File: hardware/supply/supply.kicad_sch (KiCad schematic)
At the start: 33 parts, among them J1 Conn_01x01, J2 Screw, J3 Conn_01x01, J5 Conn_01x01, J6 Screw, J7 Conn_01x01, Q3 IRF4905PBF, Q4 BC857C, Q5 IRF4905PBF, Q6 IRF4905PBF, T1 TST160 19V-19V - 727 (4.21A)

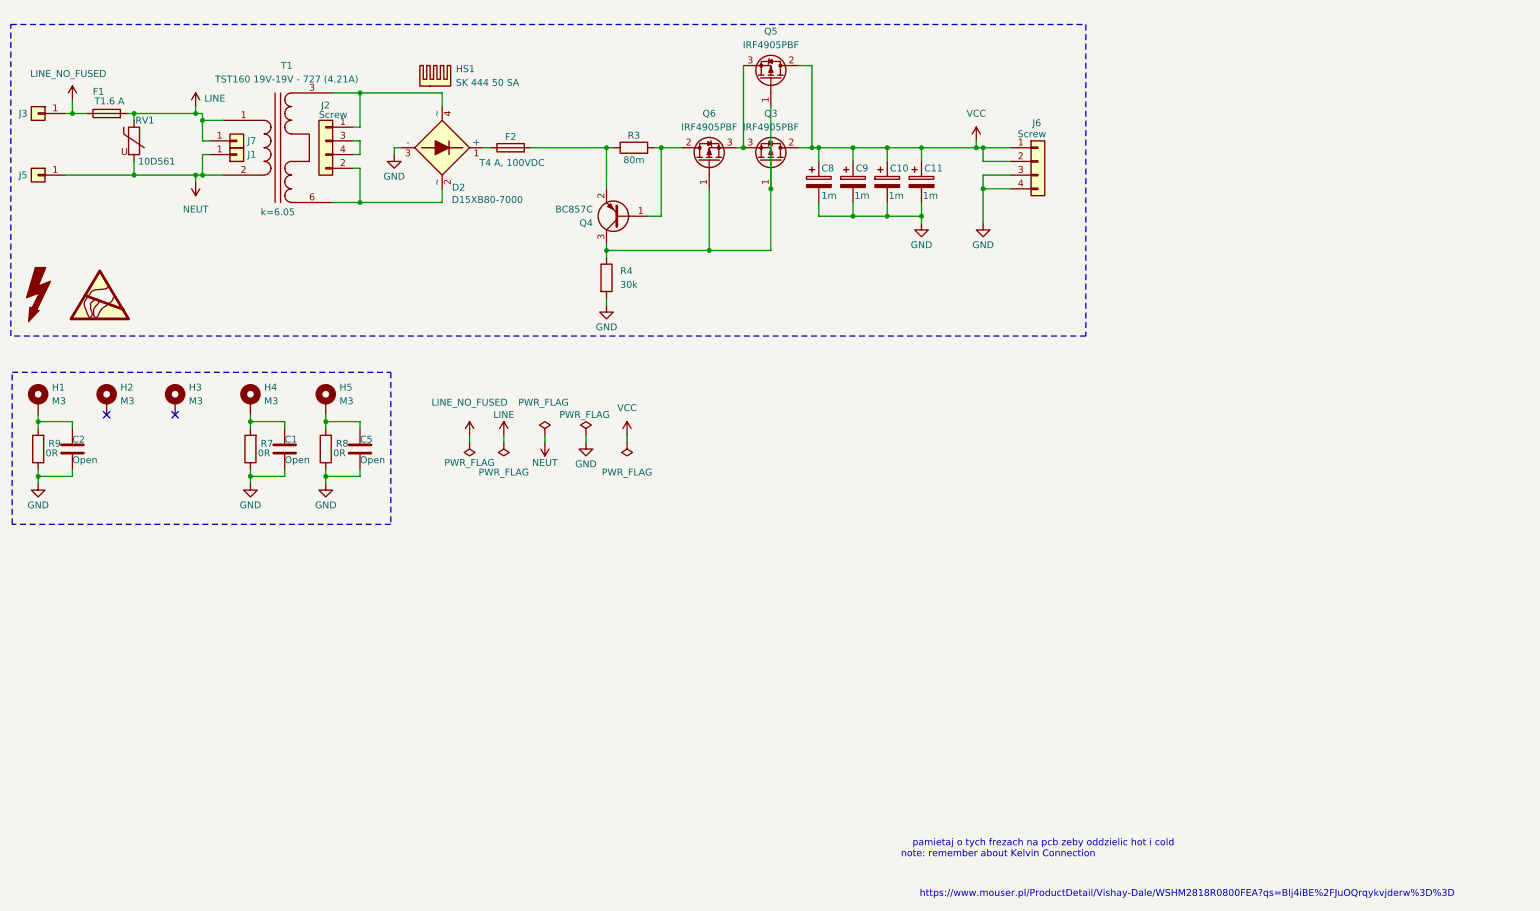
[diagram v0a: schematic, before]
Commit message: replace mosfets with bjts in inrush current limiter
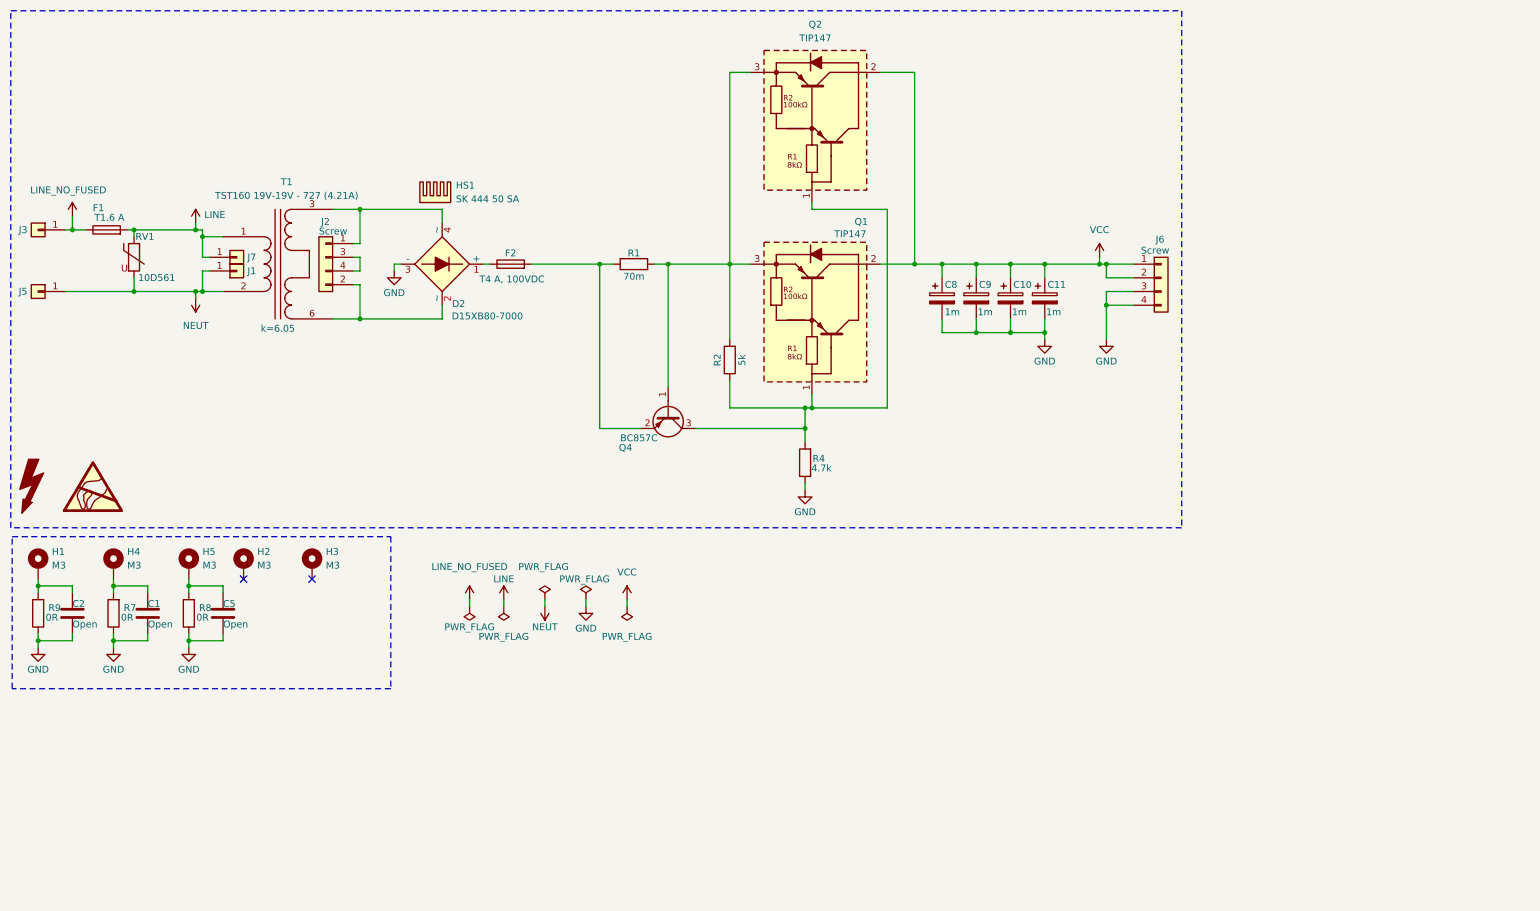
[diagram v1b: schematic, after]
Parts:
- removed Q3, Q5, Q6: IRF4905PBF, Package_TO_SOT_THT:TO-220-3_Vertical, symbol Transistor_FET:IRF4905
- removed R3: 80m, supply:WSHM28181L000FEA, symbol Device:R
- added Q1, Q2: TIP147, supply:TO545P515X1560X2445-3P, symbol supply:TIP147
- added R1: 70m, symbol Device:R
- added R2: 5k, Resistor_SMD:R_0805_2012Metric, symbol Device:R
- R4: value 30k -> 4.7k; footprint Resistor_SMD:R_1206_3216Metric -> Resistor_SMD:R_0805_2012Metric
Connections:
- net GND: now also R4.1; no longer R4.2
- net VCC: now also Q1.2 (C), Q2.2 (C)
- net at Q4.3 (C): now also R4.2, Q1.1 (B), Q2.1 (B), R2.1; no longer R4.1
- net at F2.2, Q4.2 (E): now also R1.1
- net at Q4.1 (B): now also Q1.3 (E), Q2.3 (E), R1.2, R2.2
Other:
- note removed: "https://www.mouser.pl/ProductDetail/Vishay-Dale/WSHM2818R0800FEA?qs=Blj4iBE%2FJuOQrqykvjderw%3D%3D"
- note removed: "note: remember about Kelvin Connection"
- note removed: "pamietaj o tych frezach na pcb zeby oddzielic hot i cold"
- moved on the sheet: C1, C10, C11, C2, C5, C8, C9, D2, F1, F2, H1, H2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

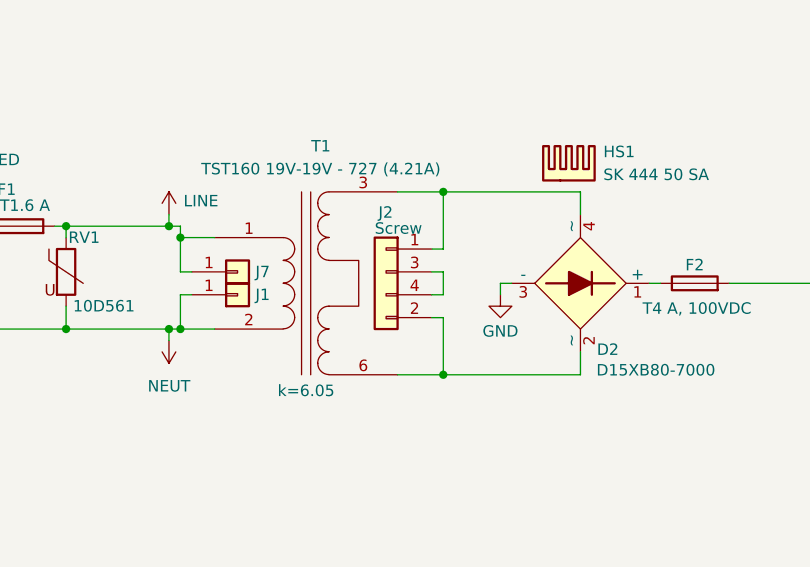
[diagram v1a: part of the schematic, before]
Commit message: swap power connectors and flip front panel PCB orientation
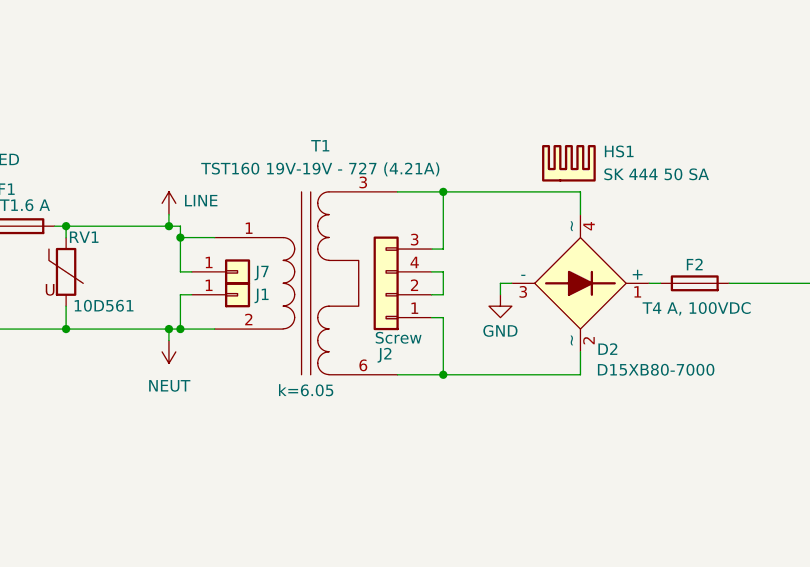
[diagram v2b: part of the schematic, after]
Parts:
- J2, J6: footprint supply:2125201004 -> supply:43045-04YY_121314
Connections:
- net at D2.4 (~~{}), T1.3 (SA): now also J2.3 (Pin_3); no longer J2.1 (Pin_1)
- net at D2.2 (~~{}), T1.6 (SD): now also J2.1 (Pin_1); no longer J2.2 (Pin_2)
- net at J2.4 (Pin_4): now also J2.2 (Pin_2); no longer J2.3 (Pin_3)
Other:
- moved on the sheet: J2
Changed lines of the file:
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@@
 	(wire
 		(pts
+			(xy 78.74 59.69) (xy 78.74 62.23)
+		)
+		(stroke
+			(width 0)
+			(type default)
+		)
+	)
+	(wire
+		(pts
 			(xy 53.34 129.54) (xy 53.34 130.81)
 		)
@@
 	(wire
 		(pts
+			(xy 77.47 57.15) (xy 78.74 57.15)
+		)
+		(stroke
+			(width 0)
+			(type default)
+		)
+	)
+	(wire
+		(pts
 			(xy 49.53 55.88) (xy 49.53 59.69)
 		)
@@
 	(wire
 		(pts
-			(xy 78.74 59.69) (xy 78.74 62.23)
-		)
-		(stroke
-			(width 0)
-			(type default)
-		)
-	)
-	(wire
-		(pts
 			(xy 101.6 60.96) (xy 102.87 60.96)
 		)
@@
 	(wire
 		(pts
-			(xy 78.74 64.77) (xy 77.47 64.77)
-		)
-		(stroke
-			(width 0)
-			(type default)
-		)
-	)
-	(wire
-		(pts
 			(xy 161.29 101.6) (xy 161.29 102.87)
 		)
@@
 	(wire
 		(pts
-			(xy 77.47 62.23) (xy 78.74 62.23)
+			(xy 77.47 64.77) (xy 78.74 64.77)
 		)
 		(stroke
@@
 	(wire
 		(pts
-			(xy 77.47 57.15) (xy 78.74 57.15)
+			(xy 77.47 59.69) (xy 78.74 59.69)
 		)
 		(stroke
@@
 	(wire
 		(pts
-			(xy 77.47 59.69) (xy 78.74 59.69)
+			(xy 77.47 62.23) (xy 78.74 62.23)
 		)
 		(stroke
@@
 			)
 		)
-		(property "Footprint" "supply:2125201004"
+		(property "Footprint" "supply:43045-04YY_121314"
 			(at 227.33 63.5 0)
 			(hide yes)
@@
 		(lib_name "Conn_01x04_1")
 		(lib_id "Connector_Generic:Conn_01x04")
-		(at 72.39 59.69 0)
-		(mirror y)
+		(at 72.39 62.23 180)
 		(unit 1)
 		(body_style 1)
@@
 		(dnp no)
 		(property "Reference" "J2"
-			(at 73.152 53.086 0)
+			(at 73.152 68.834 0)
 			(show_name no)
 			(do_not_autoplace no)
@@
 		)
 		(property "Value" "Screw"
-			(at 71.12 54.864 0)
+			(at 71.12 67.056 0)
 			(show_name no)
 			(do_not_autoplace no)
@@
 			)
 		)
-		(property "Footprint" "supply:2125201004"
-			(at 74.93 68.58 0)
+		(property "Footprint" "supply:43045-04YY_121314"
+			(at 74.93 53.34 0)
 			(hide yes)
 			(show_name no)
@@
 		)
 		(property "Datasheet" ""
-			(at 72.39 59.69 0)
+			(at 72.39 62.23 0)
 			(hide yes)
 			(show_name no)
@@
 		)
 		(property "Description" "Generic connector, single row, 01x04, script generated (kicad-library-utils/schlib/autogen/connector/)"
-			(at 74.93 68.58 0)
+			(at 74.93 53.34 0)
 			(hide yes)
 			(show_name no)
@@
 		)
 		(property "Sim.Type" ""
-			(at 72.39 59.69 0)
+			(at 72.39 62.23 0)
 			(hide yes)
 			(show_name no)
@@
 		)
 		(property "Height" ""
-			(at 72.39 59.69 0)
+			(at 72.39 62.23 0)
 			(hide yes)
 			(show_name no)
@@
 		)
 		(property "Manufacturer_Name" ""
-			(at 72.39 59.69 0)
+			(at 72.39 62.23 0)
 			(hide yes)
 			(show_name no)
@@
 		)
 		(property "Mouser Part Number" ""
-			(at 72.39 59.69 0)
+			(at 72.39 62.23 0)
 			(hide yes)
 			(show_name no)
@@
 		)
 		(property "Mouser Price/Stock" ""
-			(at 72.39 59.69 0)
+			(at 72.39 62.23 0)
 			(hide yes)
 			(show_name no)
@@
 		)
 		(property "TME Electronic Components Part Number" ""
-			(at 72.39 59.69 0)
+			(at 72.39 62.23 0)
 			(hide yes)
 			(show_name no)
@@
 		)
 		(property "TME Electronic Components Price/Stock" ""
-			(at 72.39 59.69 0)
+			(at 72.39 62.23 0)
 			(hide yes)
 			(show_name no)

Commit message: Prepare PCB for production
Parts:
- C1, C2, C5: now left out of the parts list
- F1: Manufacturer_Part_Number (none) -> 0031.8201
- F2: Manufacturer_Part_Number (none) -> 0154004.DRT
- HS1: Manufacturer_Part_Number (none) -> SK_444 5_SA
- J1, J3, J5, J7: Manufacturer_Part_Number (none) -> 726386-2
- J2, J6: Manufacturer_Part_Number (none) -> 43045-04YY_121314
- Q4: Manufacturer_Part_Number (none) -> BC857C
- R2, R4: Manufacturer_Part_Number (none) -> RC0603FR-074K7L
- R7, R8, R9: Manufacturer_Part_Number (none) -> CRCW06030000Z0EA
- RV1: Manufacturer_Part_Number (none) -> 10D561
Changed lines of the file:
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@@
 			)
 		)
+		(property "Manufacturer_Part_Number" "RC0603FR-074K7L"
+			(at 147.32 78.74 90)
+			(hide yes)
+			(show_name no)
+			(do_not_autoplace no)
+			(effects
+				(font
+					(size 1.27 1.27)
+				)
+			)
+		)
 		(pin "1"
 		)
@@
 		(body_style 1)
 		(exclude_from_sim no)
-		(in_bom yes)
+		(in_bom no)
 		(on_board yes)
 		(in_pos_files yes)
@@
 			)
 		)
+		(property "Manufacturer_Part_Number" "726386-2"
+			(at 19.05 66.04 0)
+			(hide yes)
+			(show_name no)
+			(do_not_autoplace no)
+			(effects
+				(font
+					(size 1.27 1.27)
+				)
+			)
+		)
 		(pin "1"
 		)
@@
 			)
 		)
+		(property "Manufacturer_Part_Number" "0154004.DRT"
+			(at 106.68 60.96 90)
+			(hide yes)
+			(show_name no)
+			(do_not_autoplace no)
+			(effects
+				(font
+					(size 1.27 1.27)
+				)
+			)
+		)
 		(pin "2"
 		)
@@
 			)
 		)
+		(property "Manufacturer_Part_Number" "0031.8201"
+			(at 31.75 54.61 90)
+			(hide yes)
+			(show_name no)
+			(do_not_autoplace no)
+			(effects
+				(font
+					(size 1.27 1.27)
+				)
+			)
+		)
 		(pin "2"
 		)
@@
 			)
 		)
+		(property "Manufacturer_Part_Number" "CRCW06030000Z0EA"
+			(at 19.05 125.73 0)
+			(hide yes)
+			(show_name no)
+			(do_not_autoplace no)
+			(effects
+				(font
+					(size 1.27 1.27)
+				)
+			)
+		)
 		(pin "2"
 		)
@@
 			)
 		)
+		(property "Manufacturer_Part_Number" "CRCW06030000Z0EA"
+			(at 46.99 125.73 0)
+			(hide yes)
+			(show_name no)
+			(do_not_autoplace no)
+			(effects
+				(font
+					(size 1.27 1.27)
+				)
+			)
+		)
 		(pin "2"
 		)
@@
 			)
 		)
+		(property "Manufacturer_Part_Number" "SK_444 5_SA"
+			(at 92.71 49.53 0)
+			(hide yes)
+			(show_name no)
+			(do_not_autoplace no)
+			(effects
+				(font
+					(size 1.27 1.27)
+				)
+			)
+		)
 		(instances
 			(project "supply"
@@
 			)
 		)
+		(property "Manufacturer_Part_Number" "43045-04YY_121314"
+			(at 227.33 63.5 0)
+			(hide yes)
+			(show_name no)
+			(do_not_autoplace no)
+			(effects
+				(font
+					(size 1.27 1.27)
+				)
+			)
+		)
 		(pin "3"
 		)
@@
 			)
 		)
+		(property "Manufacturer_Part_Number" "726386-2"
+			(at 55.88 62.23 0)
+			(hide yes)
+			(show_name no)
+			(do_not_autoplace no)
+			(effects
+				(font
+					(size 1.27 1.27)
+				)
+			)
+		)
 		(pin "1"
 		)
@@
 		(body_style 1)
 		(exclude_from_sim no)
-		(in_bom yes)
+		(in_bom no)
 		(on_board yes)
 		(in_pos_files yes)
@@
 			)
 		)
+		(property "Manufacturer_Part_Number" "726386-2"
+			(at 55.88 59.69 0)
+			(hide yes)
+			(show_name no)
+			(do_not_autoplace no)
+			(effects
+				(font
+					(size 1.27 1.27)
+				)
+			)
+		)
 		(pin "1"
 		)
@@
 			)
 		)
+		(property "Manufacturer_Part_Number" "43045-04YY_121314"
+			(at 72.39 62.23 0)
+			(hide yes)
+			(show_name no)
+			(do_not_autoplace no)
+			(effects
+				(font
+					(size 1.27 1.27)
+				)
+			)
+		)
 		(pin "3"
 		)
@@
 			)
 		)
+		(property "Manufacturer_Part_Number" "10D561"
+			(at 36.83 59.69 0)
+			(hide yes)
+			(show_name no)
+			(do_not_autoplace no)
+			(effects
+				(font
+					(size 1.27 1.27)
+				)
+			)
+		)
 		(pin "1"
 		)
@@
 			)
 		)
+		(property "Manufacturer_Part_Number" "BC857C"
+			(at 135.89 88.9 90)
+			(hide yes)
+			(show_name no)
+			(do_not_autoplace no)
+			(effects
+				(font
+					(size 1.27 1.27)
+				)
+			)
+		)
 		(pin "3"
 		)
@@
 			)
 		)
+		(property "Manufacturer_Part_Number" "726386-2"
+			(at 19.05 54.61 0)
+			(hide yes)
+			(show_name no)
+			(do_not_autoplace no)
+			(effects
+				(font
+					(size 1.27 1.27)
+				)
+			)
+		)
 		(pin "1"
 		)
@@
 			)
 		)
+		(property "Manufacturer_Part_Number" "RC0603FR-074K7L"
+			(at 161.29 97.79 0)
+			(hide yes)
+			(show_name no)
+			(do_not_autoplace no)
+			(effects
+				(font
+					(size 1.27 1.27)
+				)
+			)
+		)
 		(pin "1"
 		)
@@
 			)
 		)
+		(property "Manufacturer_Part_Number" "CRCW06030000Z0EA"
+			(at 33.02 125.73 0)
+			(hide yes)
+			(show_name no)
+			(do_not_autoplace no)
+			(effects
+				(font
+					(size 1.27 1.27)
+				)
+			)
+		)
 		(pin "2"
 		)
@@
 		(body_style 1)
 		(exclude_from_sim no)
-		(in_bom yes)
+		(in_bom no)
 		(on_board yes)
 		(in_pos_files yes)
